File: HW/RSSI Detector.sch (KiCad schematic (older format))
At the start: 30 parts, among them P1 SMA, P2 SMA, U1 AD8319, U2 AD8319, U3 Teensy3.2

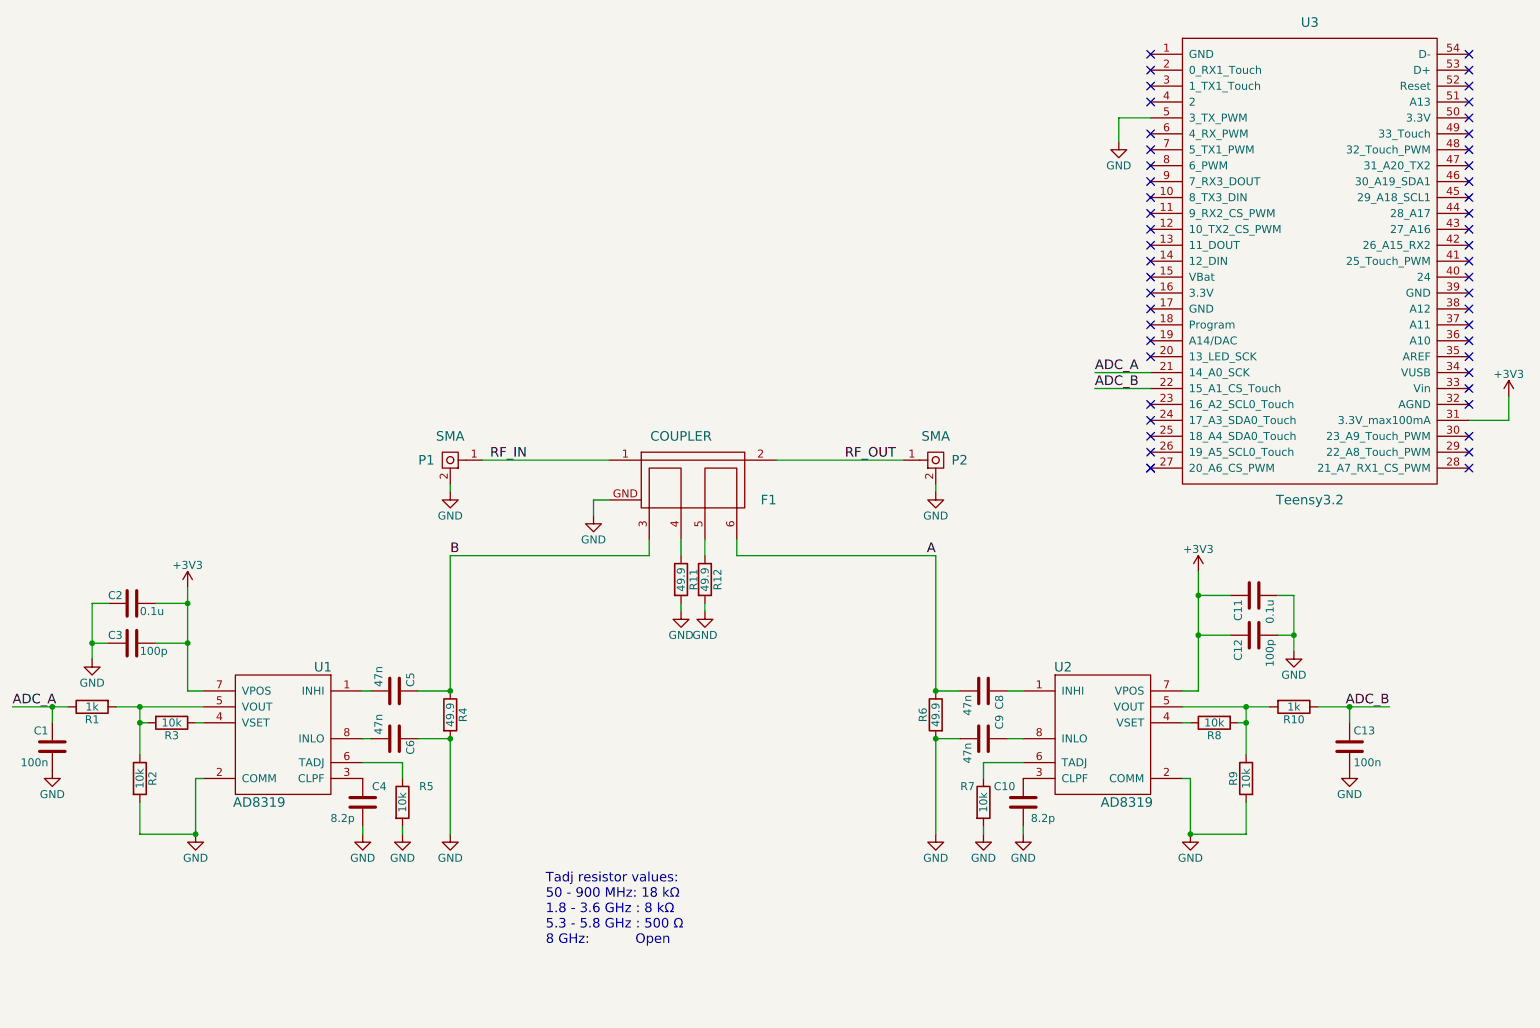
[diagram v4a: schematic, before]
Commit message: added temp adj transistor switch
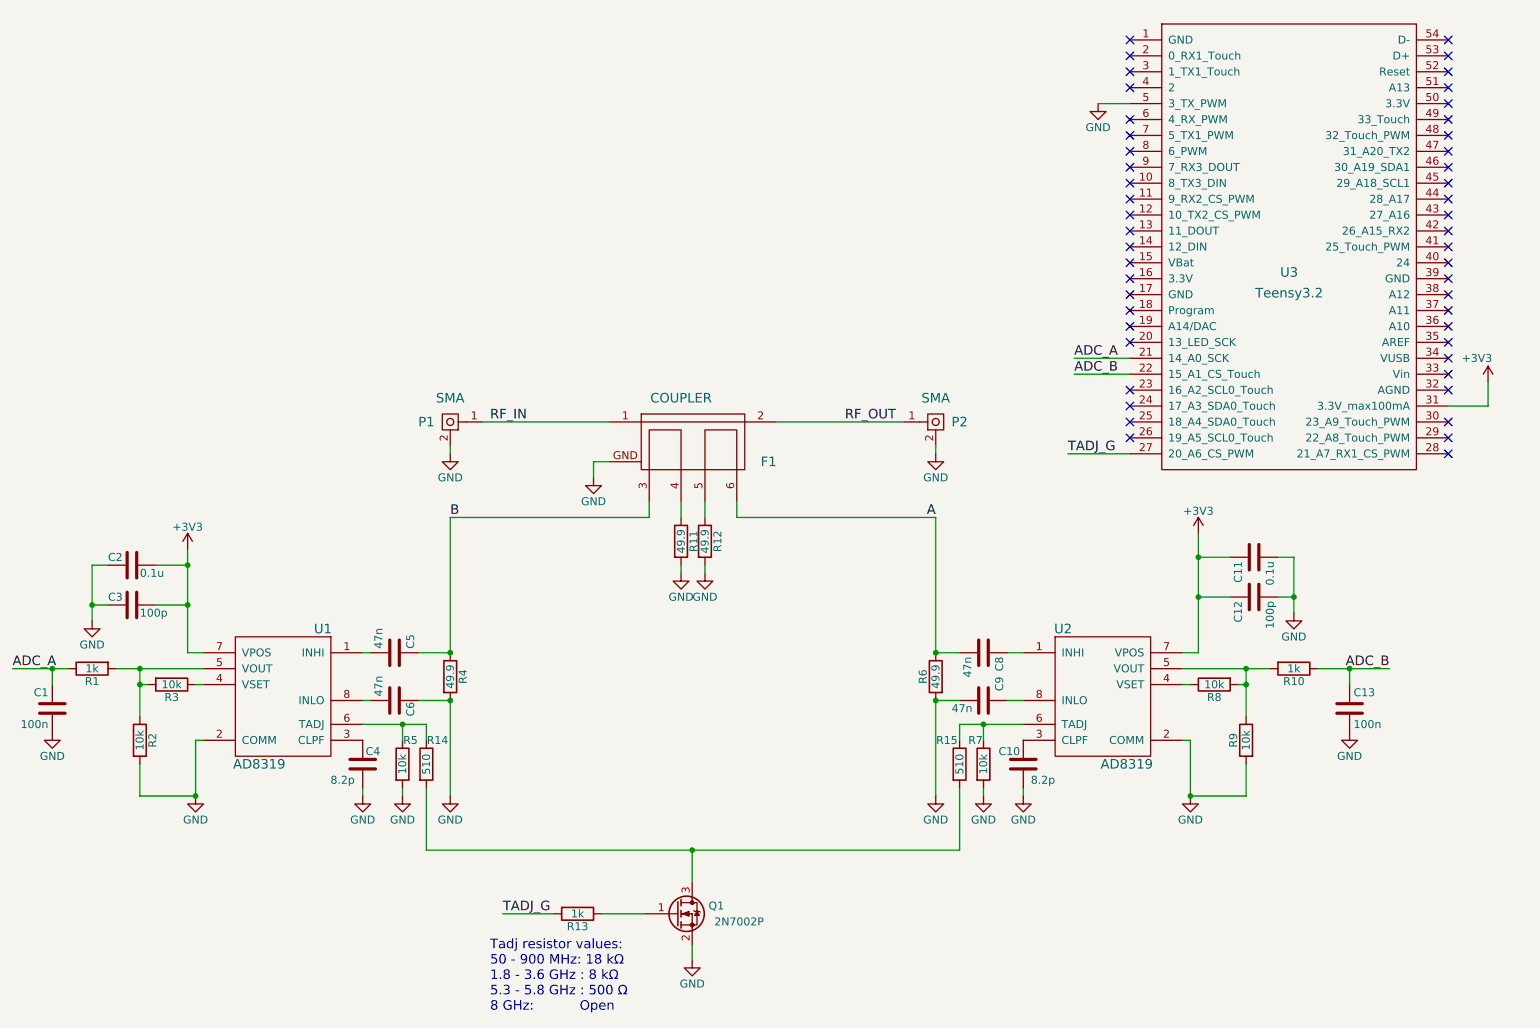
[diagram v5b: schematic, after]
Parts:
- added Q1: 2N7002P, TO_SOT_Packages_SMD:SOT-23, symbol Q_NMOS_GSD
- added R13: 1k, Resistors_SMD:R_0603, symbol R
- added R14, R15: 510, Resistors_SMD:R_0603, symbol R
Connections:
- net GND: now also Q1.2 (S)
- net at R5.1, U1.6 (TADJ): now also R14.1
- net at R7.1, U2.6 (TADJ): now also R15.1
- net TADJ_G: now reaches U3.27 (20_A6_CS_PWM)
- net TADJ_G: now also R13.2
- new net: Q1.3 (D), R14.2, R15.2
- new net: Q1.1 (G), R13.1
- no-connect marks 51 -> 49
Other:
- moved on the sheet: C1, C10, C11, C12, C13, C2, C3, C4, C5, C6, C8, C9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
